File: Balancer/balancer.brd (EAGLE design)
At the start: 139.7 x 325.1 mm, 322 parts, among them Q1 BSS123W, Q10A SIR882DP-T1-GE3, Q10B SIS468DN-T1-GE3, Q11A SIR882DP-T1-GE3, Q11B SIS468DN-T1-GE3, Q12A SIR882DP-T1-GE3, Q12B SIS468DN-T1-GE3, Q1A8 SIR882DP-T1-GE3, Q1B8 SIS468DN-T1-GE3, Q2 BSS123W, Q3A SIR882DP-T1-GE3, Q3B SIS468DN-T1-GE3, Q4 MMBT3906LT1G, Q4A SIR882DP-T1-GE3, Q4B SIS468DN-T1-GE3, Q5 FDN5618P, Q5A SIR882DP-T1-GE3, Q5B SIS468DN-T1-GE3, Q6 CMPT3904E_TR_PBFREE, Q6A SIR882DP-T1-GE3, Q6B SIS468DN-T1-GE3, Q9A SIR882DP-T1-GE3, Q9B SIS468DN-T1-GE3, T10 750312504, T11 750312504, T12 750312504, T3 750312504, T4 750312504, T5 750312504, T6 750312504, T8 750312504, T9 750312504, U1 LTC3300ILXE-1PBF, U2 LTC3300ILXE-1PBF

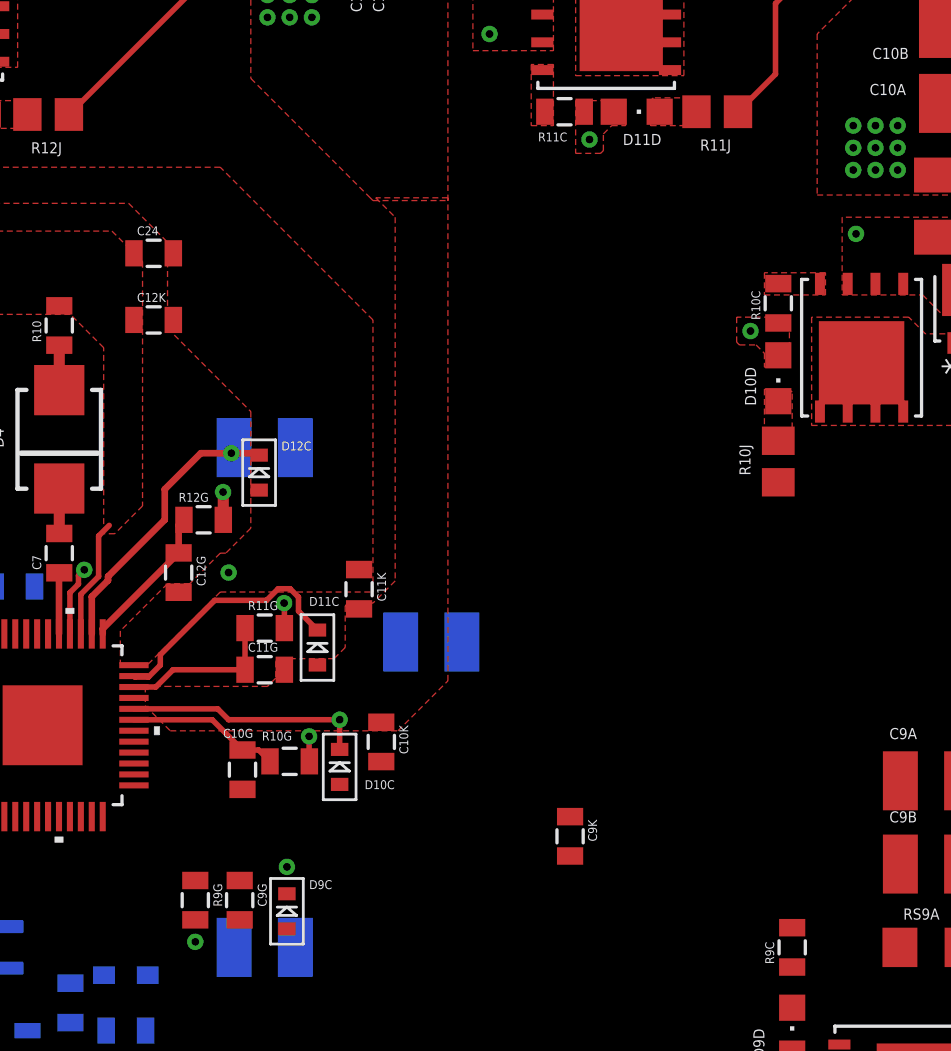
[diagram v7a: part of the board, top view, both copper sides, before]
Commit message: made traces on L1 of PCB
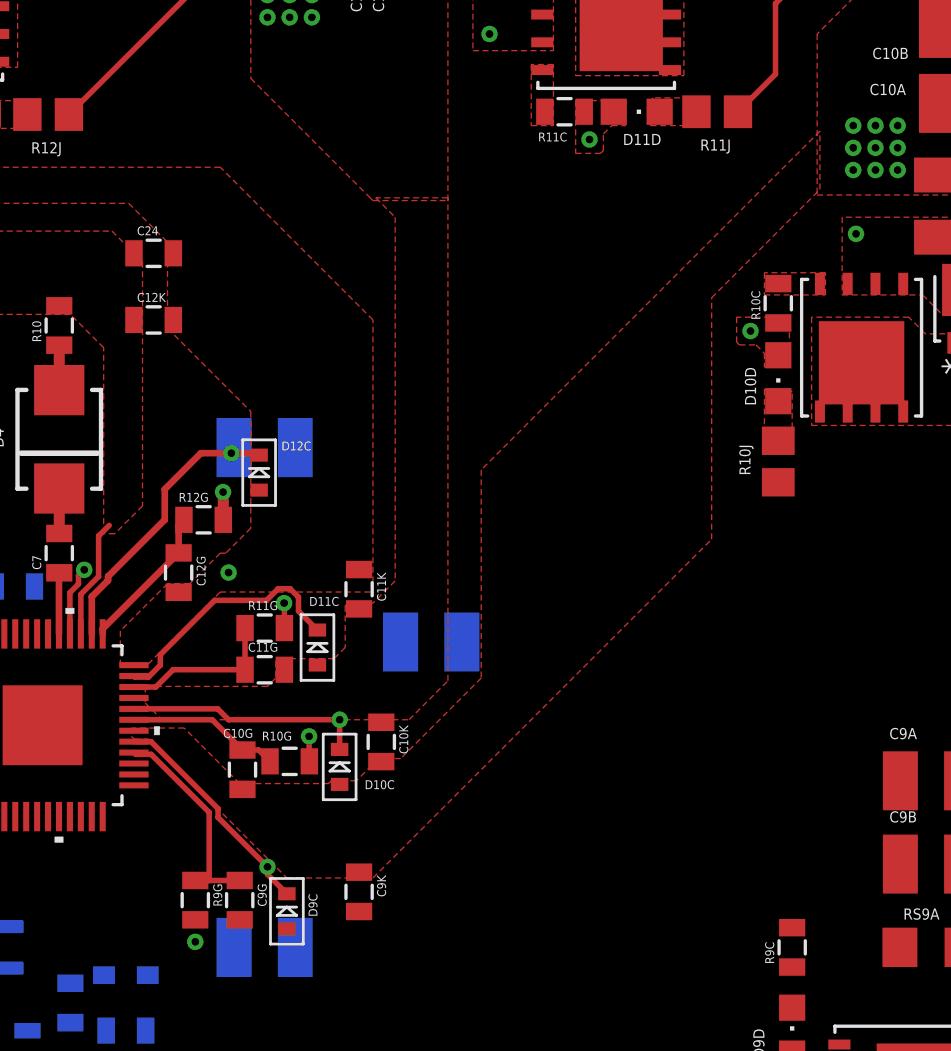
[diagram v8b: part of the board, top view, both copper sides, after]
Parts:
- moved C9K 9.98 mm to (42.4, 234.9)
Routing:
- net G9P: track 0.00 -> 10.3 mm, vias 0 -> 1
- net I9P: track 0.00 -> 9.72 mm
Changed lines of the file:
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@@
 <attribute name="VALUE" x="14.859" y="240.284" size="0.4064" layer="27" rot="R90"/>
 </element>
-<element name="C9K" library="Ilya_Teach" package="0805" value="1uF" x="52.07" y="237.49" smashed="yes" rot="R270">
-<attribute name="NAME" x="52.8955" y="238.252" size="0.4064" layer="25" rot="R270"/>
-<attribute name="VALUE" x="50.673" y="238.506" size="0.4064" layer="27" rot="R270"/>
+<element name="C9K" library="Ilya_Teach" package="0805" value="1uF" x="42.418" y="234.95" smashed="yes" rot="R270">
+<attribute name="NAME" x="43.2435" y="235.712" size="0.4064" layer="25" rot="R270"/>
+<attribute name="VALUE" x="41.021" y="235.966" size="0.4064" layer="27" rot="R270"/>
 </element>
 <element name="C9M" library="Ilya_Teach" package="0805" value="10nF" x="105.41" y="111.76" smashed="yes">
@@
 </element>
 <element name="D9C" library="adafruit" package="SOD-523" value="" x="39.116" y="234.061" smashed="yes">
-<attribute name="NAME" x="40.132" y="235.077" size="0.4064" layer="25"/>
+<attribute name="NAME" x="40.513" y="233.807" size="0.4064" layer="25" rot="R90"/>
 <attribute name="VALUE" x="40.132" y="232.537" size="0.4064" layer="27"/>
 </element>
@@
 <wire x1="30.75" y1="231.14" x2="26.46" y2="233.36" width="0" layer="19" extent="16-16"/>
 <wire x1="36.7" y1="232.41" x2="30.75" y2="231.14" width="0" layer="19" extent="16-16"/>
+<wire x1="42.418" y1="234.05" x2="36.7" y2="232.41" width="0" layer="19" extent="1-16"/>
 <wire x1="15.24" y1="233.31" x2="13.462" y2="240.4" width="0" layer="19" extent="1-1"/>
 <wire x1="17.78" y1="233.31" x2="15.24" y2="233.31" width="0" layer="19" extent="1-1"/>
 <wire x1="14.34" y1="252.73" x2="17.907" y2="245.48" width="0" layer="19" extent="1-1"/>
 <wire x1="21.59" y1="256.67" x2="14.34" y2="252.73" width="0" layer="19" extent="1-1"/>
-<wire x1="44.32" y1="246.38" x2="32.1183" y2="240.82" width="0" layer="19" extent="1-16"/>
-<wire x1="52.07" y1="236.59" x2="44.32" y2="246.38" width="0" layer="19" extent="1-16"/>
+<wire x1="44.32" y1="246.38" x2="42.418" y2="234.05" width="0" layer="19" extent="1-16"/>
 <wire x1="9.6" y1="200.7" x2="15.24" y2="233.31" width="0" layer="19" extent="1-1"/>
 <wire x1="9.6" y1="198.2" x2="9.6" y2="200.7" width="0" layer="19" extent="1-1"/>
@@
 <wire x1="32.12" y1="167.64" x2="25.4" y2="171.82" width="0" layer="19" extent="1-1"/>
 <wire x1="27.15" y1="159.1183" x2="32.12" y2="167.64" width="0" layer="19" extent="1-1"/>
-<wire x1="96.368" y1="234.95" x2="52.07" y2="236.59" width="0" layer="19" extent="1-1"/>
+<wire x1="18.796" y1="306.073" x2="21.59" y2="256.67" width="0" layer="19" extent="1-1"/>
+<wire x1="46.38" y1="306.832" x2="19.558" y2="308.61" width="0" layer="19" extent="1-1"/>
+<wire x1="96.368" y1="234.95" x2="44.32" y2="246.38" width="0" layer="19" extent="1-16"/>
 <wire x1="97.92" y1="231.14" x2="96.368" y2="234.95" width="0" layer="19" extent="1-1"/>
 <wire x1="98.933" y1="262.89" x2="96.368" y2="234.95" width="0" layer="19" extent="1-1"/>
@@
 <wire x1="119.38" y1="181.46" x2="107.4928" y2="196.85" width="0" layer="19" extent="16-16"/>
 <wire x1="119.51" y1="170.18" x2="119.38" y2="181.46" width="0" layer="19" extent="16-16"/>
-<wire x1="18.796" y1="306.073" x2="21.59" y2="256.67" width="0" layer="19" extent="1-1"/>
-<wire x1="46.38" y1="306.832" x2="19.558" y2="308.61" width="0" layer="19" extent="1-1"/>
 <wire x1="109.54" y1="106.68" x2="119.51" y2="170.18" width="0" layer="19" extent="1-16"/>
 </signal>
@@
 <contactref element="D9D" pad="A"/>
 <contactref element="U2" pad="29"/>
+<via x="38.227" y="236.093" extent="1-16" drill="0.35"/>
+<wire x1="39.116" y1="234.861" x2="38.227" y2="235.75" width="0.254" layer="1"/>
+<wire x1="38.227" y1="235.75" x2="38.227" y2="236.093" width="0.254" layer="1"/>
+<wire x1="38.227" y1="236.093" x2="35.9664" y2="238.3536" width="0.254" layer="1"/>
+<wire x1="35.9664" y1="238.3536" x2="35.9664" y2="238.75456875" width="0.254" layer="1"/>
+<wire x1="35.9664" y1="238.75456875" x2="32.90096875" y2="241.82" width="0.254" layer="1"/>
+<wire x1="32.90096875" y1="241.82" x2="32.1183" y2="241.82" width="0.254" layer="1"/>
 <wire x1="62.23" y1="227.55" x2="62.23" y2="231.51" width="0" layer="19" extent="1-1"/>
 <wire x1="39.116" y1="234.861" x2="62.23" y2="231.51" width="0" layer="19" extent="1-1"/>
-<wire x1="32.1183" y1="241.82" x2="39.116" y2="234.861" width="0" layer="19" extent="1-1"/>
 </signal>
 <signal name="C8">
@@
 <contactref element="C9G" pad="1"/>
 <contactref element="U2" pad="28"/>
-<wire x1="34.925" y1="235.469" x2="32.1183" y2="241.32" width="0" layer="19" extent="1-1"/>
-<wire x1="36.957" y1="235.469" x2="34.925" y2="235.469" width="0" layer="19" extent="1-1"/>
+<wire x1="36.957" y1="235.469" x2="35.56" y2="235.469" width="0.254" layer="1"/>
+<wire x1="35.56" y1="235.469" x2="34.925" y2="235.469" width="0.254" layer="1"/>
+<wire x1="32.1183" y1="241.32" x2="32.1992" y2="241.2391" width="0.254" layer="1"/>
+<wire x1="32.1992" y1="241.2391" x2="32.90713125" y2="241.2391" width="0.254" layer="1"/>
+<wire x1="32.90713125" y1="241.2391" x2="35.56" y2="238.58623125" width="0.254" layer="1"/>
+<wire x1="35.56" y1="238.58623125" x2="35.56" y2="235.469" width="0.254" layer="1"/>
 </signal>
 <signal name="N$79">
@@
 <vertex x="69.723" y="266.827"/>
 </polygon>
+<polygon width="0.1524" layer="1" isolate="0.127" thermals="no">
+<vertex x="32.004" y="242.443"/>
+<vertex x="32.004" y="242.062"/>
+<vertex x="32.131" y="241.935"/>
+<vertex x="32.766" y="241.935"/>
+<vertex x="39.116" y="235.585"/>
+<vertex x="43.053" y="235.585"/>
+<vertex x="58.547" y="251.079"/>
+<vertex x="58.547" y="262.128"/>
+<vertex x="63.5" y="267.081"/>
+<vertex x="63.5" y="269.748"/>
+<vertex x="48.006" y="254.254"/>
+<vertex x="48.006" y="244.729"/>
+<vertex x="44.323" y="241.046"/>
+<vertex x="43.307" y="241.046"/>
+<vertex x="42.291" y="240.03"/>
+<vertex x="41.148" y="240.03"/>
+<vertex x="41.021" y="239.903"/>
+<vertex x="36.957" y="239.903"/>
+<vertex x="34.417" y="242.443"/>
+</polygon>
 <wire x1="110.9472" y1="213.36" x2="109.54" y2="111.76" width="0" layer="19" extent="1-1"/>
 <wire x1="119.38" y1="222.1" x2="110.9472" y2="213.36" width="0" layer="19" extent="16-16"/>
@@
 <wire x1="61.595" y1="253.685" x2="67.18" y2="240.03" width="0" layer="19" extent="1-1"/>
 <wire x1="65.024" y1="267.97" x2="61.595" y2="253.685" width="0" layer="19" extent="1-1"/>
-<wire x1="52.07" y1="238.39" x2="67.18" y2="240.03" width="0" layer="19" extent="1-1"/>
-<wire x1="43.434" y1="240.908" x2="52.07" y2="238.39" width="0" layer="19" extent="1-1"/>
-<wire x1="41.529" y1="239.865" x2="43.434" y2="240.908" width="0" layer="19" extent="1-1"/>
-<wire x1="37.084" y1="239.638" x2="41.529" y2="239.865" width="0" layer="19" extent="1-1"/>
-<wire x1="32.1183" y1="242.32" x2="37.084" y2="239.638" width="0" layer="19" extent="1-1"/>
-<wire x1="39.5" y1="232.41" x2="37.084" y2="239.638" width="0" layer="19" extent="1-16"/>
+<wire x1="39.5" y1="232.41" x2="42.418" y2="235.85" width="0" layer="19" extent="1-16"/>
 <wire x1="36.7" y1="255.27" x2="32.1183" y2="242.32" width="0" layer="19" extent="1-16"/>
 </signal>
@@
 <vertex x="38.608" y="244.729"/>
 <vertex x="38.227" y="244.348"/>
-<vertex x="33.782" y="244.348"/>
 <vertex x="32.639" y="244.348"/>
-<vertex x="32.639" y="243.459"/>
-<vertex x="33.782" y="242.316"/>
-<vertex x="44.196" y="242.316"/>
+<vertex x="32.639" y="243.586"/>
+<vertex x="33.401" y="242.824"/>
+<vertex x="44.704" y="242.824"/>
 <vertex x="46.482" y="244.602"/>
 <vertex x="46.482" y="266.7"/>
@@
 <wire x1="104.51" y1="96.52" x2="106.36" y2="99.06" width="0" layer="19" extent="1-1"/>
 </signal>
-<signal name="N$66">
-<via x="39.116" y="236.093" extent="1-16" drill="0.35"/>
-</signal>
 <signal name="N$69">
